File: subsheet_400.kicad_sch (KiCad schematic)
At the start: 13 parts, among them J1901 ROM[0..6] Breakout, U400 STE_GSTMCU_PHY

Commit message: pcb session 2023-01-21T22:41:51+01:00
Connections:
- net GND: now also U400.73 (GND), U400.74 (TEST)
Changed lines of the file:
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@@
     (stroke (width 0) (type default) (color 0 0 0 0))
+  )
+  (label "GND" (at 180.34 162.56 180)
+    (effects (font (size 1.27 1.27)) (justify right bottom))
   )
   (label "D11" (at 177.8 147.32 180)
@@
     (pin "99")
   )
-  (symbol (lib_id "Device:C") (at 27.94 184.15 0)
+  (symbol (lib_id "Device:C") (at 27.94 184.15 0) (unit 1)
     (in_bom yes) (on_board yes)
     (property "Reference" "C402" (id 0) (at 28.575 181.61 0)
@@
     (pin "2")
   )
-  (symbol (lib_id "Device:C") (at 40.64 184.15 0)
+  (symbol (lib_id "Device:C") (at 40.64 184.15 0) (unit 1)
     (in_bom yes) (on_board yes)
     (property "Reference" "C403" (id 0) (at 41.275 181.61 0)
@@
     (pin "2")
   )
-  (symbol (lib_id "Device:C") (at 27.94 209.55 0)
+  (symbol (lib_id "Device:C") (at 27.94 209.55 0) (unit 1)
     (in_bom yes) (on_board yes)
     (property "Reference" "C404" (id 0) (at 28.575 207.01 0)
@@
     (pin "2")
   )
-  (symbol (lib_id "Device:C") (at 40.64 209.55 0)
+  (symbol (lib_id "Device:C") (at 40.64 209.55 0) (unit 1)
     (in_bom yes) (on_board yes)
     (property "Reference" "C405" (id 0) (at 41.275 207.01 0)
@@
     (pin "2")
   )
-  (symbol (lib_id "Device:C") (at 27.94 234.95 0)
+  (symbol (lib_id "Device:C") (at 27.94 234.95 0) (unit 1)
     (in_bom yes) (on_board yes)
     (property "Reference" "C406" (id 0) (at 28.575 232.41 0)
@@
     (pin "2")
   )
-  (symbol (lib_id "Device:R_Small_US") (at 175.26 190.5 270)
+  (symbol (lib_id "Device:R_Small_US") (at 175.26 190.5 270) (unit 1)
     (in_bom yes) (on_board yes)
     (property "Reference" "R421" (id 0) (at 175.26 187.96 90))

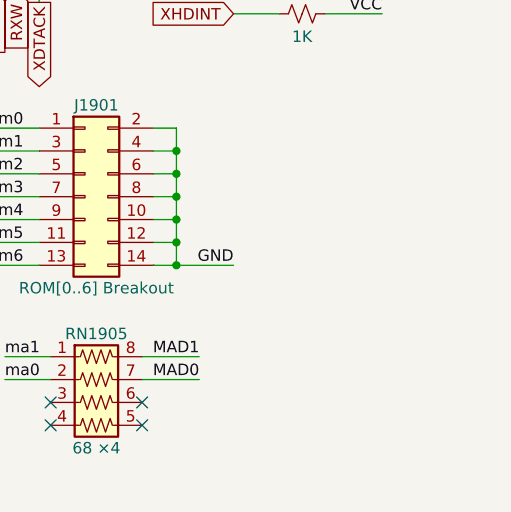
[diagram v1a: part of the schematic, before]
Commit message: add gnd/vcc symbol to start replacing local labels
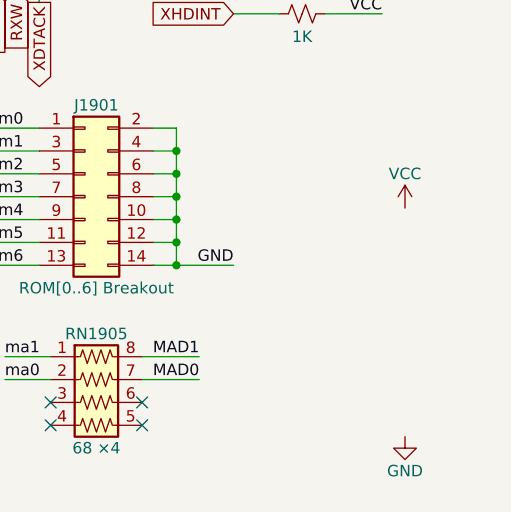
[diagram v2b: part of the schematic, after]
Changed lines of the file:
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@@
     (pin "9")
   )
+  (symbol (lib_id "power:VCC") (at 186.69 212.09 0) (unit 1)
+    (in_bom yes) (on_board yes)
+    (property "Reference" "#PWR?" (id 0) (at 186.69 215.9 0)
+      (effects (font (size 1.27 1.27)) hide)
+    )
+    (property "Value" "VCC" (id 1) (at 186.69 208.28 0))
+    (property "Footprint" "" (id 2) (at 186.69 212.09 0)
+      (effects (font (size 1.27 1.27)) hide)
+    )
+    (property "Datasheet" "" (id 3) (at 186.69 212.09 0)
+      (effects (font (size 1.27 1.27)) hide)
+    )
+    (pin "1")
+  )
+  (symbol (lib_id "power:GND") (at 186.69 237.49 0) (unit 1)
+    (in_bom yes) (on_board yes)
+    (property "Reference" "#PWR?" (id 0) (at 186.69 243.84 0)
+      (effects (font (size 1.27 1.27)) hide)
+    )
+    (property "Value" "GND" (id 1) (at 186.69 241.3 0))
+    (property "Footprint" "" (id 2) (at 186.69 237.49 0)
+      (effects (font (size 1.27 1.27)) hide)
+    )
+    (property "Datasheet" "" (id 3) (at 186.69 237.49 0)
+      (effects (font (size 1.27 1.27)) hide)
+    )
+    (pin "1")
+  )
 )
